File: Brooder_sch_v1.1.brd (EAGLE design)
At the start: 90 x 75 mm, 30 parts, among them J1 DCJ0202, J2 1X2-3.5MM, J3 DCJ0202, J4 1X2-3.5MM, U1 328P

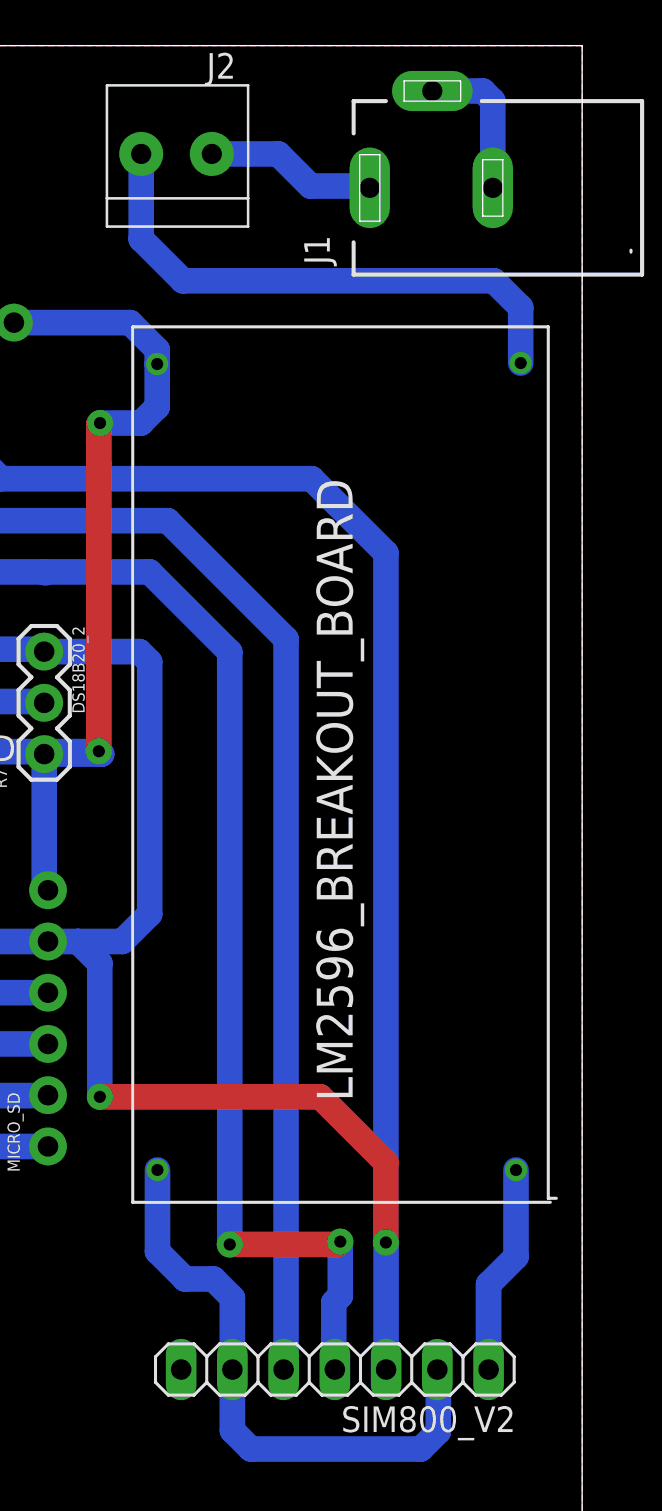
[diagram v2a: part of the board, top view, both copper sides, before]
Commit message: Increases gms power supply track from 1.27mm to 2mm
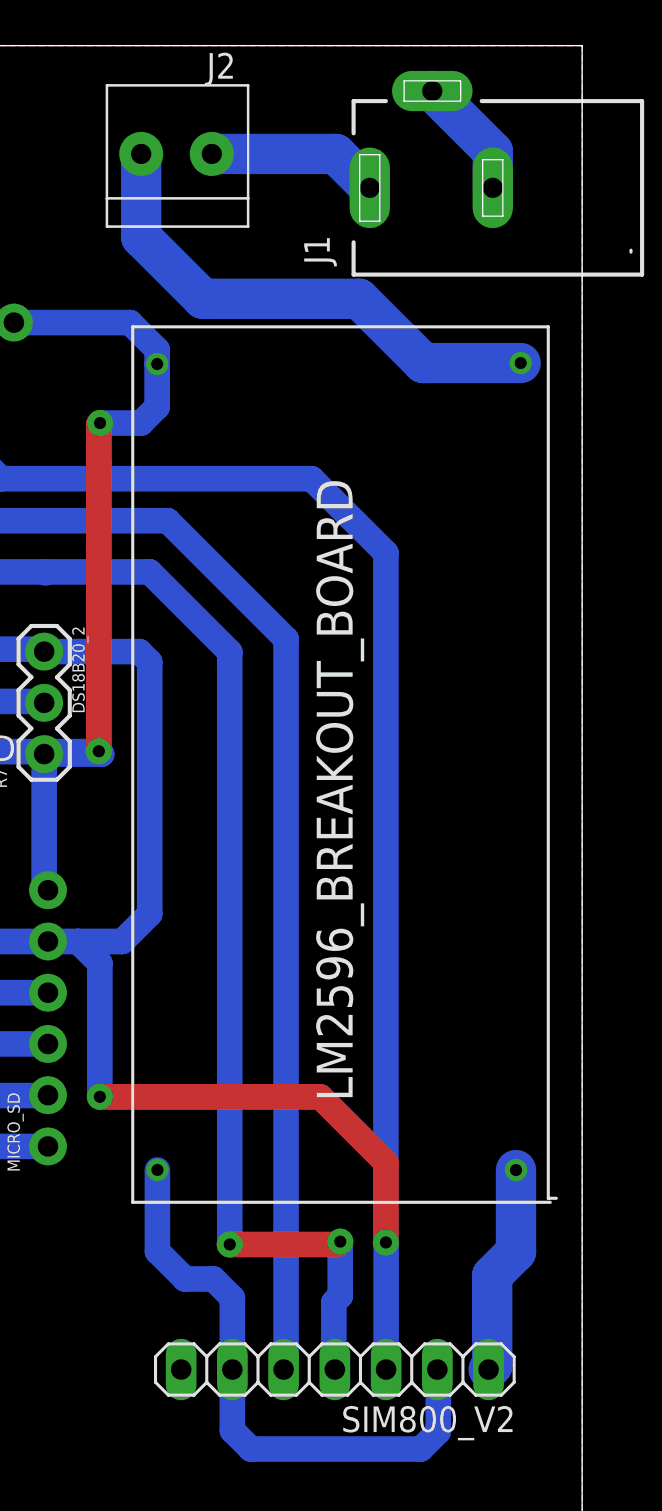
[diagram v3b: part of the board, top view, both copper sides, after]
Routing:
- net 12V_S_SIM: track 27.2 -> 25.5 mm
- net GND: track 235.6 -> 234.2 mm
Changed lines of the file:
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@@
 <wire x1="39.29" y1="41.29" x2="41.94" y2="41.29" width="1.27" layer="16"/>
 <wire x1="36.75" y1="38.75" x2="39.29" y2="41.29" width="1.27" layer="16"/>
-<wire x1="85.57" y1="67.95" x2="85.57" y2="72.26" width="1.27" layer="16"/>
-<wire x1="85.57" y1="72.26" x2="85.08" y2="72.75" width="1.27" layer="16"/>
-<wire x1="85.08" y1="72.75" x2="82.57" y2="72.75" width="1.27" layer="16"/>
 <wire x1="4.31" y1="52.87" x2="2.57" y2="52.87" width="1.27" layer="16"/>
 <wire x1="2.57" y1="52.87" x2="2.07" y2="53.37" width="1.27" layer="16"/>
@@
 <wire x1="2.77" y1="63.03" x2="4.31" y2="63.03" width="1.27" layer="16"/>
 <wire x1="2.07" y1="62.33" x2="2.77" y2="63.03" width="1.27" layer="16"/>
+<wire x1="85.57" y1="67.95" x2="85.57" y2="69.75" width="2" layer="16"/>
+<wire x1="85.57" y1="69.75" x2="82.57" y2="72.75" width="2" layer="16"/>
+<wire x1="68.9319125" y1="59.9280875" x2="85.57" y2="67.95" width="0" layer="19" extent="16-16"/>
+<wire x1="52.47" y1="40.32" x2="56.04" y2="40" width="0" layer="19" extent="16-16"/>
+<wire x1="19.71" y1="34.8" x2="19.72" y2="39.62" width="0" layer="19" extent="1-1"/>
+<wire x1="13.87" y1="52.87" x2="20.24" y2="41.49" width="0" layer="19" extent="1-16"/>
+<wire x1="68.945340625" y1="19.264259375" x2="63.52" y2="33.13" width="0" layer="19" extent="1-1"/>
+<wire x1="4.31" y1="24.93" x2="19.71" y2="34.8" width="0" layer="19" extent="1-1"/>
+<wire x1="14.67" y1="14.96" x2="9" y2="15" width="0" layer="19" extent="1-1"/>
+<wire x1="5" y1="7" x2="4.19" y2="14.85" width="0" layer="19" extent="16-16"/>
+<wire x1="54" y1="3.73" x2="46" y2="3.75" width="0" layer="19" extent="1-1"/>
+<wire x1="34.4888" y1="66.7906" x2="15.02" y2="66.32" width="0" layer="19" extent="1-1"/>
 </signal>
 <signal name="12V">
@@
 <contactref element="U$2" pad="OUT(+VE)"/>
 <contactref element="SIM800_V2" pad="1"/>
-<wire x1="86.72" y1="19.26" x2="86.72" y2="14.96" width="1.27" layer="16"/>
-<wire x1="85.36" y1="13.6" x2="85.36" y2="9.37" width="1.27" layer="16"/>
-<wire x1="86.72" y1="14.96" x2="85.36" y2="13.6" width="1.27" layer="16"/>
+<wire x1="86.72" y1="19.26" x2="86.72" y2="15.21" width="2" layer="16"/>
+<wire x1="86.72" y1="15.21" x2="85.54" y2="14.03" width="2" layer="16"/>
+<wire x1="85.54" y1="14.03" x2="85.54" y2="9.55" width="2" layer="16"/>
+<wire x1="85.54" y1="9.55" x2="85.36" y2="9.37" width="2" layer="16"/>
 </signal>
 <signal name="12V_SIM">
 <contactref element="J1" pad="1"/>
 <contactref element="J2" pad="1"/>
-<wire x1="79.47" y1="67.95" x2="79.38" y2="68.04" width="1.27" layer="16"/>
-<wire x1="79.38" y1="68.04" x2="76.53" y2="68.04" width="1.27" layer="16"/>
-<wire x1="76.53" y1="68.04" x2="74.94" y2="69.63" width="1.27" layer="16"/>
-<wire x1="74.94" y1="69.63" x2="71.64" y2="69.63" width="1.27" layer="16"/>
+<wire x1="71.64" y1="69.63" x2="77.79" y2="69.63" width="2" layer="16"/>
+<wire x1="77.79" y1="69.63" x2="79.47" y2="67.95" width="2" layer="16"/>
 </signal>
 <signal name="12V_S_SIM">
 <contactref element="J2" pad="2"/>
 <contactref element="U$2" pad="IN(+VE)"/>
-<wire x1="68.14" y1="69.63" x2="68.14" y2="65.41" width="1.27" layer="16"/>
-<wire x1="86.95318125" y1="62.01681875" x2="86.95318125" y2="59.265190625" width="1.27" layer="16"/>
-<wire x1="68.14" y1="65.41" x2="70.21" y2="63.34" width="1.27" layer="16"/>
-<wire x1="70.21" y1="63.34" x2="85.63" y2="63.34" width="1.27" layer="16"/>
-<wire x1="85.63" y1="63.34" x2="86.95318125" y2="62.01681875" width="1.27" layer="16"/>
+<wire x1="68.14" y1="69.63" x2="68.14" y2="65.51" width="2" layer="16"/>
+<wire x1="71.2" y1="62.45" x2="78.94" y2="62.45" width="2" layer="16"/>
+<wire x1="78.94" y1="62.45" x2="82.124809375" y2="59.265190625" width="2" layer="16"/>
+<wire x1="82.124809375" y1="59.265190625" x2="86.95318125" y2="59.265190625" width="2" layer="16"/>
+<wire x1="68.14" y1="65.51" x2="71.2" y2="62.45" width="2" layer="16"/>
 </signal>
 </signals>

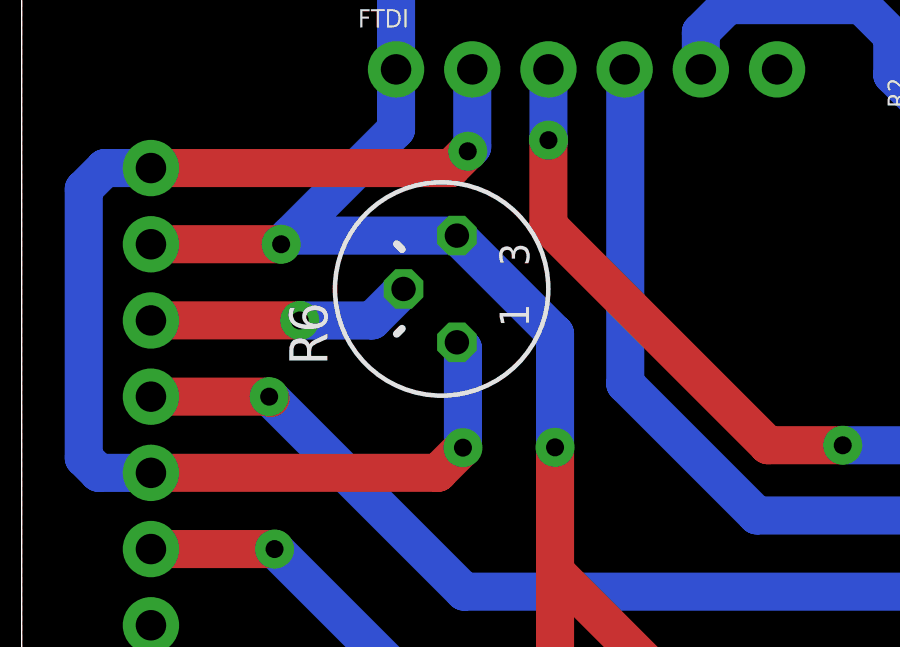
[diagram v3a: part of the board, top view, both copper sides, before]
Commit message: Replaces pot rj6 with pot ct6
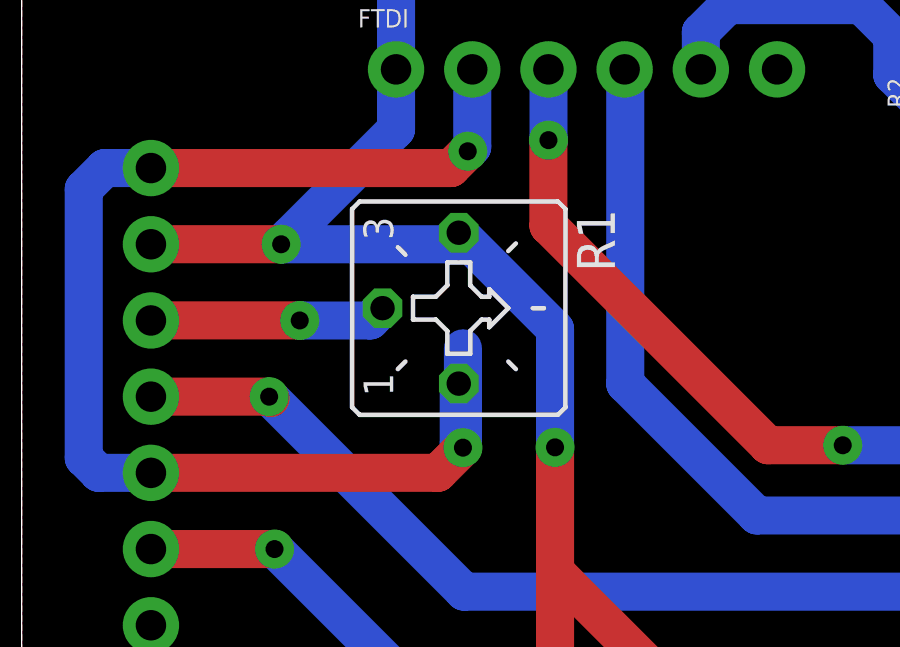
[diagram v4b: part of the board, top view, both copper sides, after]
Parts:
- removed R6: (no value), pot:RJ6
- added R1: (no value), pot:CT6
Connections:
- net 5V: now also R1.E; no longer R6.E
- net GND: now also R1.A; no longer R6.A
- net VO: now also R1.S; no longer R6.S
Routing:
- net GND: track 234.2 -> 236.1 mm
- net VO: track 8.85 -> 7.89 mm
- net 5V: track 376.2 -> 376.7 mm
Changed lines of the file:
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@@
 </element>
 <element name="TEST_LED" library="adafruit" package="LED5MM" value="" x="51" y="39"/>
-<element name="R6" library="pot" library_urn="urn:adsk.eagle:library:331" package="RJ6" package3d_urn="urn:adsk.eagle:package:22699/1" value="" x="14" y="59" rot="R90"/>
 <element name="DS3231" library="SparkFun-Connectors" package="1X06_NO_SILK" value="" x="49.13" y="61.27">
 <attribute name="PROD_ID" value="CONN-08437" x="49.13" y="61.27" size="1.778" layer="27" display="off"/>
@@
 <element name="LED1" library="adafruit" package="LED5MM" value="" x="54" y="5" rot="R270"/>
 <element name="J4" library="adafruit" package="1X2-3.5MM" value="1X2-3.5MM" x="18" y="5" rot="R180"/>
+<element name="R1" library="pot" library_urn="urn:adsk.eagle:library:331" package="CT6" package3d_urn="urn:adsk.eagle:package:22692/1" value="" x="14.57" y="58.36" rot="R270"/>
 </elements>
 <signals>
@@
 <contactref element="FTDI" pad="2"/>
 <contactref element="TEST_LED" pad="K"/>
-<contactref element="R6" pad="A"/>
 <contactref element="DS3231" pad="6"/>
 <wire x1="4.31" y1="63.03" x2="14.31" y2="63.03" width="1.27" layer="1"/>
@@
 <via x="14.71" y="53.71" extent="1-16" drill="0.6" diameter="1.3"/>
 <wire x1="14.71" y1="53.71" x2="14.71" y2="57.02" width="1.27" layer="16"/>
-<wire x1="14.71" y1="57.02" x2="14.508" y2="57.222" width="1.27" layer="16"/>
 <wire x1="52.47" y1="40.32" x2="52.47" y2="39.2" width="1.27" layer="16"/>
 <wire x1="52.47" y1="39.2" x2="52.27" y2="39" width="1.27" layer="16"/>
@@
 <wire x1="85.57" y1="67.95" x2="85.57" y2="69.75" width="2" layer="16"/>
 <wire x1="85.57" y1="69.75" x2="82.57" y2="72.75" width="2" layer="16"/>
-<wire x1="68.9319125" y1="59.9280875" x2="85.57" y2="67.95" width="0" layer="19" extent="16-16"/>
-<wire x1="52.47" y1="40.32" x2="56.04" y2="40" width="0" layer="19" extent="16-16"/>
-<wire x1="19.71" y1="34.8" x2="19.72" y2="39.62" width="0" layer="19" extent="1-1"/>
-<wire x1="13.87" y1="52.87" x2="20.24" y2="41.49" width="0" layer="19" extent="1-16"/>
-<wire x1="68.945340625" y1="19.264259375" x2="63.52" y2="33.13" width="0" layer="19" extent="1-1"/>
-<wire x1="4.31" y1="24.93" x2="19.71" y2="34.8" width="0" layer="19" extent="1-1"/>
-<wire x1="14.67" y1="14.96" x2="9" y2="15" width="0" layer="19" extent="1-1"/>
-<wire x1="5" y1="7" x2="4.19" y2="14.85" width="0" layer="19" extent="16-16"/>
-<wire x1="54" y1="3.73" x2="46" y2="3.75" width="0" layer="19" extent="1-1"/>
-<wire x1="34.4888" y1="66.7906" x2="15.02" y2="66.32" width="0" layer="19" extent="1-1"/>
+<contactref element="R1" pad="A"/>
+<wire x1="14.57" y1="55.8454" x2="14.57" y2="53.85" width="1.27" layer="16"/>
+<wire x1="14.57" y1="53.85" x2="14.71" y2="53.71" width="1.27" layer="16"/>
 </signal>
 <signal name="12V">
@@
 <wire x1="13.02" y1="70.89" x2="28.95" y2="70.89" width="1.27" layer="16"/>
 <wire x1="28.95" y1="70.89" x2="30.49" y2="69.35" width="1.27" layer="16"/>
-<contactref element="R6" pad="E"/>
 <contactref element="DS3231" pad="5"/>
 <via x="8.65" y="60.49" extent="1-16" drill="0.6" diameter="1.3"/>
 <wire x1="8.65" y1="60.49" x2="8.938" y2="60.778" width="1.27" layer="16"/>
-<wire x1="8.938" y1="60.778" x2="14.508" y2="60.778" width="1.27" layer="16"/>
 <wire x1="8.65" y1="60.49" x2="12.48" y2="64.32" width="1.27" layer="16"/>
 <wire x1="34.32" y1="41.29" x2="31.47" y2="41.29" width="1.27" layer="16"/>
@@
 <wire x1="17.78" y1="49.59" x2="17.78" y2="53.72" width="1.27" layer="1"/>
 <via x="17.78" y="53.72" extent="1-16" drill="0.6" diameter="1.3"/>
-<wire x1="17.78" y1="53.72" x2="17.78" y2="57.506" width="1.27" layer="16"/>
-<wire x1="17.78" y1="57.506" x2="14.508" y2="60.778" width="1.27" layer="16"/>
 <wire x1="26.1" y1="41.27" x2="17.78" y2="49.59" width="1.27" layer="1"/>
 <wire x1="4.31" y1="27.47" x2="7.54" y2="27.47" width="1.27" layer="1"/>
@@
 <wire x1="59.29" y1="61.27" x2="59.29" y2="70.03" width="1.27" layer="16"/>
 <wire x1="59.29" y1="70.03" x2="58.43" y2="70.89" width="1.27" layer="16"/>
+<contactref element="R1" pad="E"/>
+<wire x1="8.65" y1="60.49" x2="14.1854" y2="60.49" width="1.27" layer="16"/>
+<wire x1="14.1854" y1="60.49" x2="14.57" y2="60.8746" width="1.27" layer="16"/>
+<wire x1="14.57" y1="60.8746" x2="17.78" y2="57.6646" width="1.27" layer="16"/>
+<wire x1="17.78" y1="57.6646" x2="17.78" y2="53.72" width="1.27" layer="16"/>
 </signal>
 <signal name="N$4">
@@
 <contactref element="1602_LCD" pad="14"/>
 <wire x1="4.31" y1="57.95" x2="9.27" y2="57.95" width="1.27" layer="1"/>
-<contactref element="R6" pad="S"/>
 <via x="9.27" y="57.95" extent="1-16" drill="0.6" diameter="1.3"/>
-<wire x1="9.27" y1="57.95" x2="11.68" y2="57.95" width="1.27" layer="16"/>
-<wire x1="11.68" y1="57.95" x2="12.73" y2="59" width="1.27" layer="16"/>
+<contactref element="R1" pad="S"/>
+<wire x1="9.27" y1="57.95" x2="11.62" y2="57.95" width="1.27" layer="16"/>
+<wire x1="11.62" y1="57.95" x2="12.03" y2="58.36" width="1.27" layer="16"/>
 </signal>
 <signal name="PD2">
